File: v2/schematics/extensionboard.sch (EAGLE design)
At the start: 23 parts, among them IC1 TXS0104E, IC2 TXS0104E, IC3 TXS0104E, IC4 TXS0104E, IC5 TXS0104E_ENA, J1 Raspberry Pi 3, J10 RPi_GPIO_2, J11 I2C_2, J12 SPI1_5V, J13 SDA1_5V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

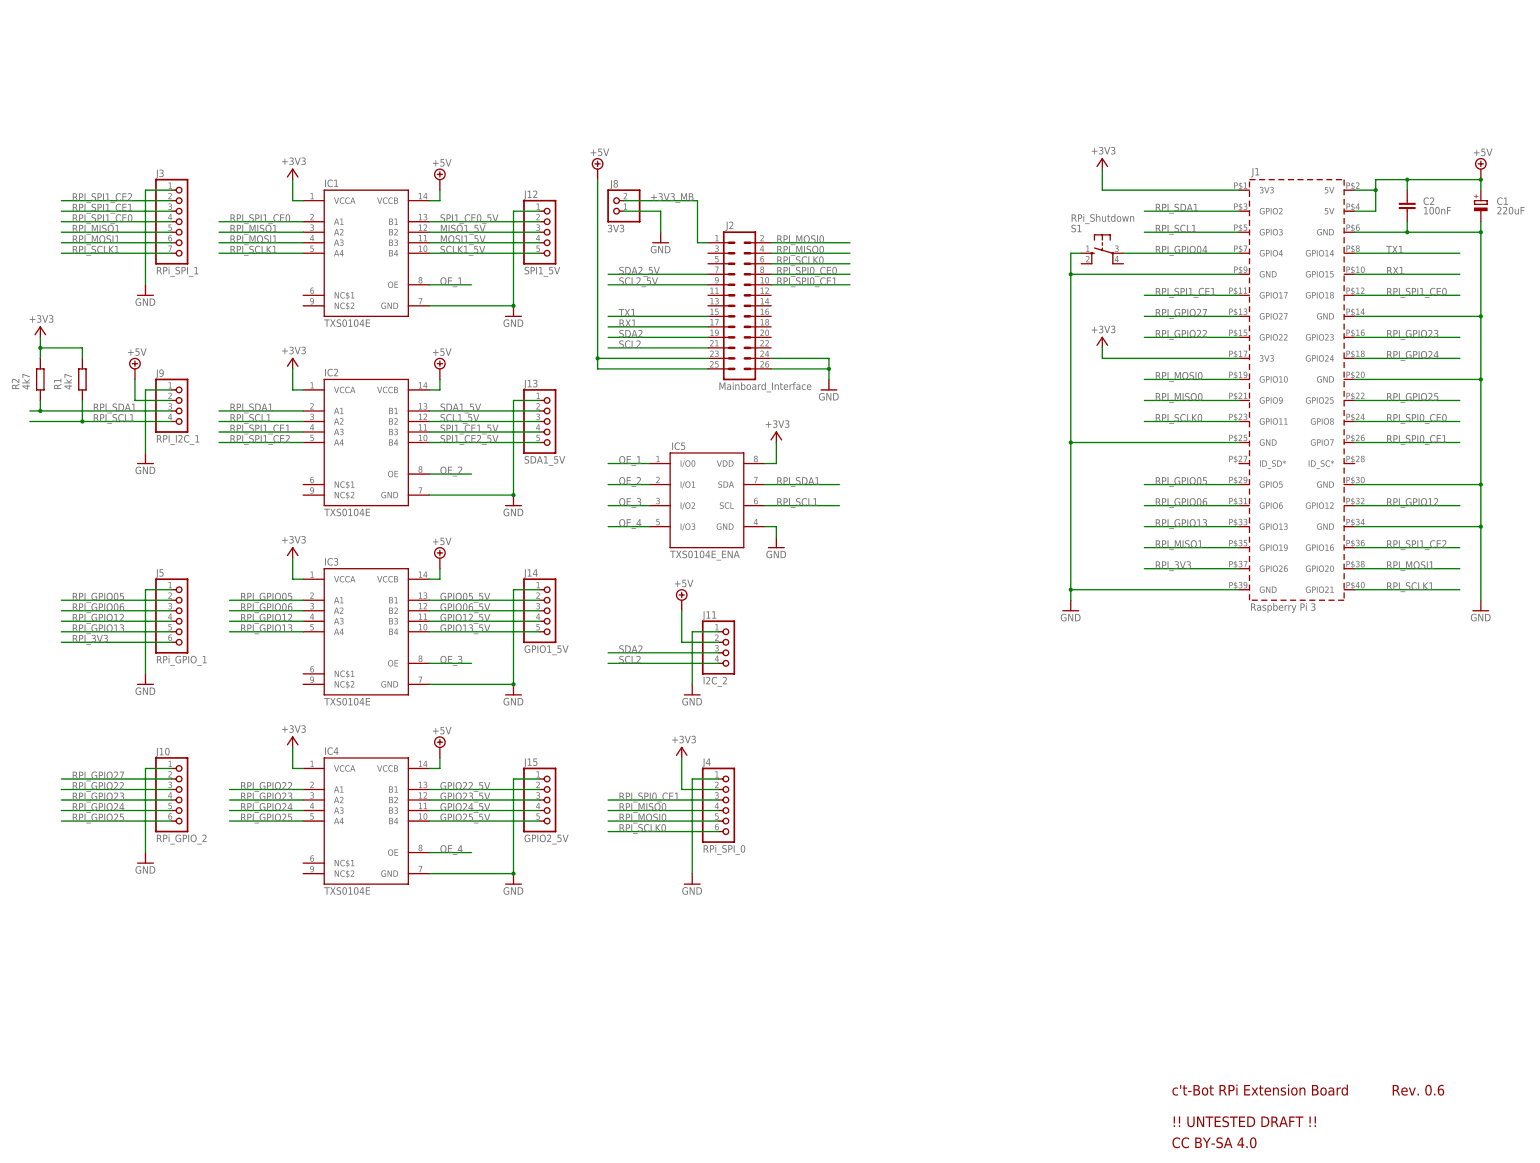
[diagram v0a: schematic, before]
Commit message: ct-bot v2 schematic updated
 - bugfix for library references, non-managed libraries added as dedicated library (ct-bot.lbr)
 - wrong footprints reverted
 - bufix for wrong signals for servo supplies
 - bugfix reverse polarity protection
 - bugifx for line sensor voltage levels
 - small smd parts exchanged with TH alternatives (bs108, mcp101) (untested)
 - distance and transport box sensors updated with I2C (untested)
 - led driver updated for up to 25 mA per channel (untested)
 - audio amp switched to pam8403 (untested)
 - bugfix for ESP12 programming mode (circuit still incomplete)
 - missing signals on RPi interface header restored
 - spi header for additional channels added due to pin mapping sheet changes
 - missing header for uart5 added
 - several layout improvements
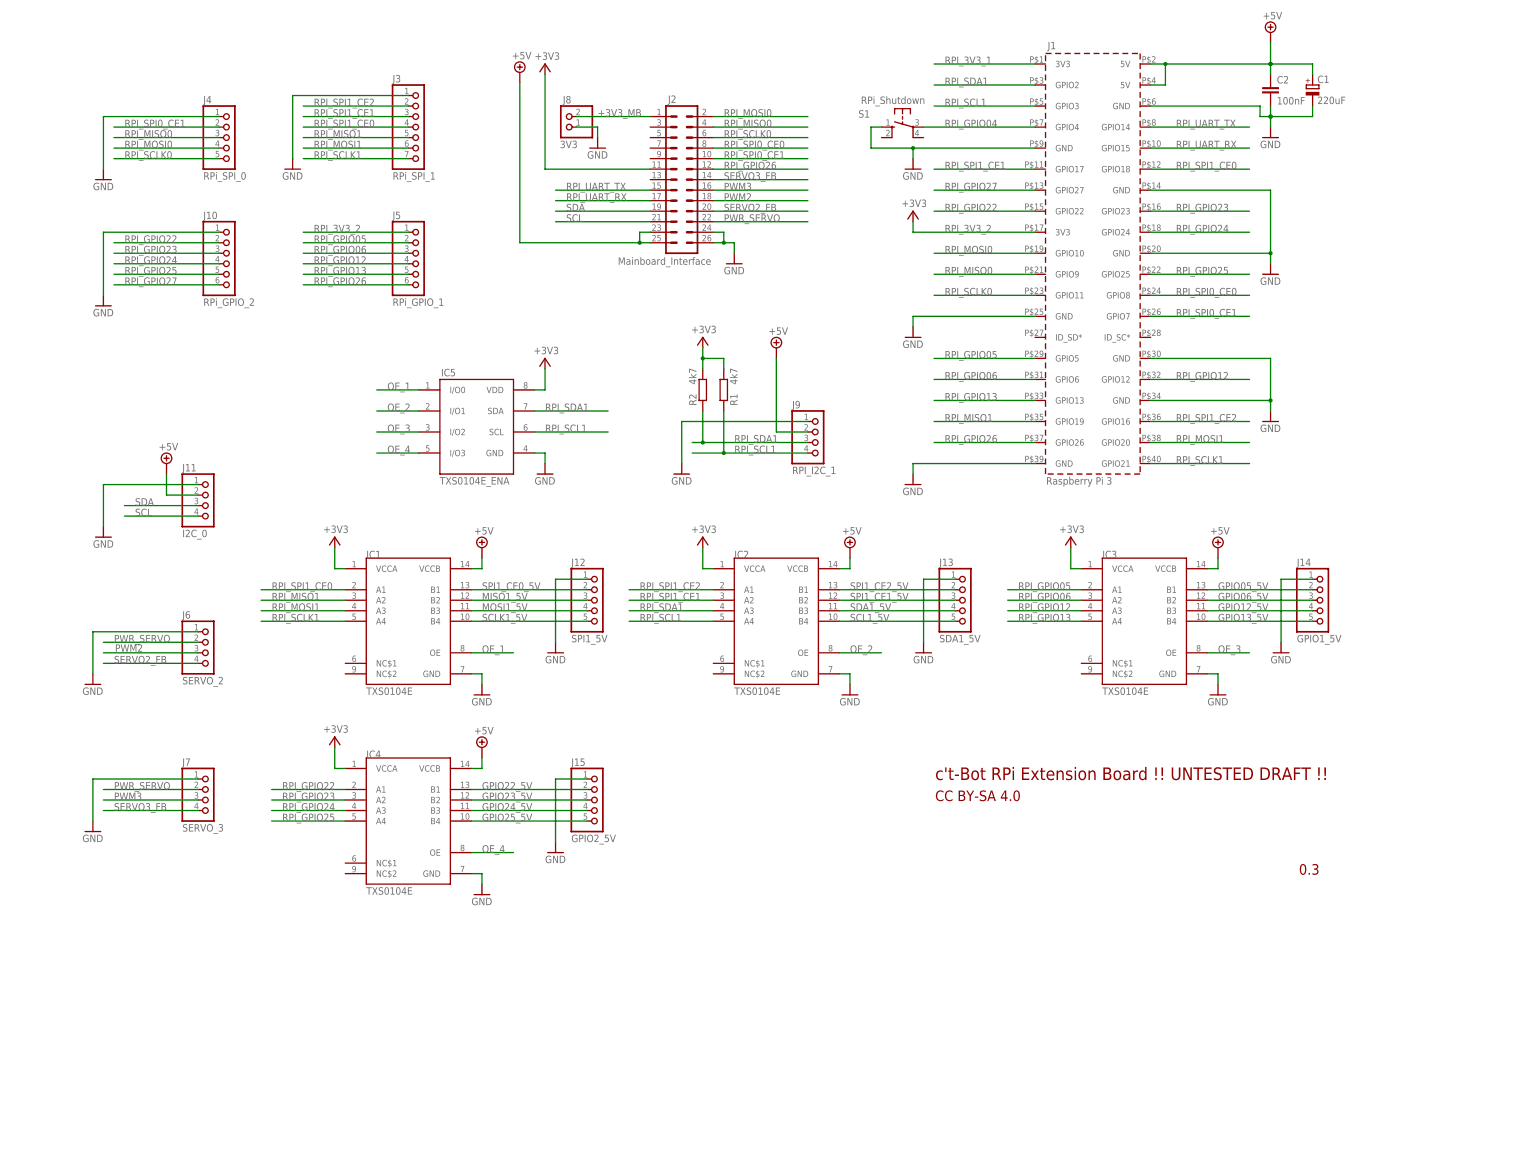
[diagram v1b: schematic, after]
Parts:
- added J6: SERVO_2, pinhead_ts:PINHD-1X4
- added J7: SERVO_3, pinhead_ts:PINHD-1X4
- J10, J5: device DIYmodules-pinhead:PINHD-1X6 -> pinhead_ts:PINHD-1X6
- J11: value I2C_2 -> I2C_0; device DIYmodules-pinhead:PINHD-1X4 -> pinhead_ts:PINHD-1X4
- J12, J13, J14, J15: device DIYmodules-pinhead:PINHD-1X5 -> pinhead_ts:PINHD-1X5
- J3: device DIYmodules-pinhead:PINHD-1X7 -> pinhead_ts:PINHD-1X7
- J4: device DIYmodules-pinhead:PINHD-1X6 -> pinhead_ts:PINHD-1X5
- J8: device DIYmodules-pinhead:PINHD-1X2 -> pinhead_ts:PINHD-1X2
- J9: device DIYmodules-pinhead:PINHD-1X4 -> pinhead_ts:PINHD-1X4
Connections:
- net N$1 renamed +3V3_MB
- net N$13 renamed SPI1_CE1_5V
- net N$14 renamed SDA1_5V
- net RX1 renamed RPI_UART_RX
- net SCL2 renamed SCL
- net SDA2 renamed SDA
- net TX1 renamed RPI_UART_TX
- removed net N$10: IC2.A2
- removed net N$11: IC2.A3
- removed net N$12: IC2.A4
- removed net N$2: J2.7
- removed net N$3: J2.9
- removed net N$4: J10.2
- removed net N$5: J10.3
- removed net N$6: J10.4
- removed net N$7: J10.5
- removed net N$8: J10.6
- removed net N$9: IC2.A1
- removed net RPI_3V3: J1.GPIO26, J5.6
- new net PWM2: J2.18, J6.3
- new net PWM3: J2.16, J7.3
- new net PWR_SERVO: J2.22, J6.2, J7.2
- new net RPI_GPIO26: J1.GPIO26, J2.12, J5.6
- new net SERVO2_FB: J2.20, J6.4
- new net SERVO3_FB: J2.14, J7.4
- net GND: now also J6.1, J7.1; no longer J5.1
- net RPI_3V3_1: no longer J4.2
- net RPI_3V3_2: now also J2.11, J5.1
- net RPI_GPIO22: now also J10.2
- net RPI_GPIO23: now also J10.3
- net RPI_GPIO24: now also J10.4
- net RPI_GPIO25: now also J10.5
- net RPI_GPIO27: now also J10.6
- net RPI_MISO0: now also J4.3; no longer J4.4
- net RPI_MOSI0: now also J4.4; no longer J4.5
- net RPI_SCL1: now also IC2.A4
- net RPI_SCLK0: now also J4.5; no longer J4.6
- net RPI_SDA1: now also IC2.A3
- net RPI_SPI0_CE1: now also J4.2; no longer J4.3
- net RPI_SPI1_CE1: now also IC2.A2
- net RPI_SPI1_CE2: now also IC2.A1
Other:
- note added: "0.3"
- note removed: "+3V3_MB"
- note removed: "RPI_GPIO22"
- note removed: "RPI_GPIO23"
- note removed: "RPI_GPIO24"
- note removed: "RPI_GPIO25"
- note removed: "RPI_GPIO27"
- note removed: "RPI_SCL1"
- note removed: "RPI_SDA1"
- note removed: "RPI_SPI1_CE1"
- note removed: "RPI_SPI1_CE2"
- note removed: "Rev. 0.6"
- note removed: "SCL1_5V"
- note removed: "SCL2_5V"
- note removed: "SDA1_5V"
- note removed: "SDA2_5V"
- note removed: "SPI1_CE1_5V"
- note removed: "SPI1_CE2_5V"
- moved on the sheet: C1, C2, IC1, IC2, IC3, IC4, IC5, J1, J10, J11, J12, J13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

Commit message: Updated schematics to Revision 0.6.
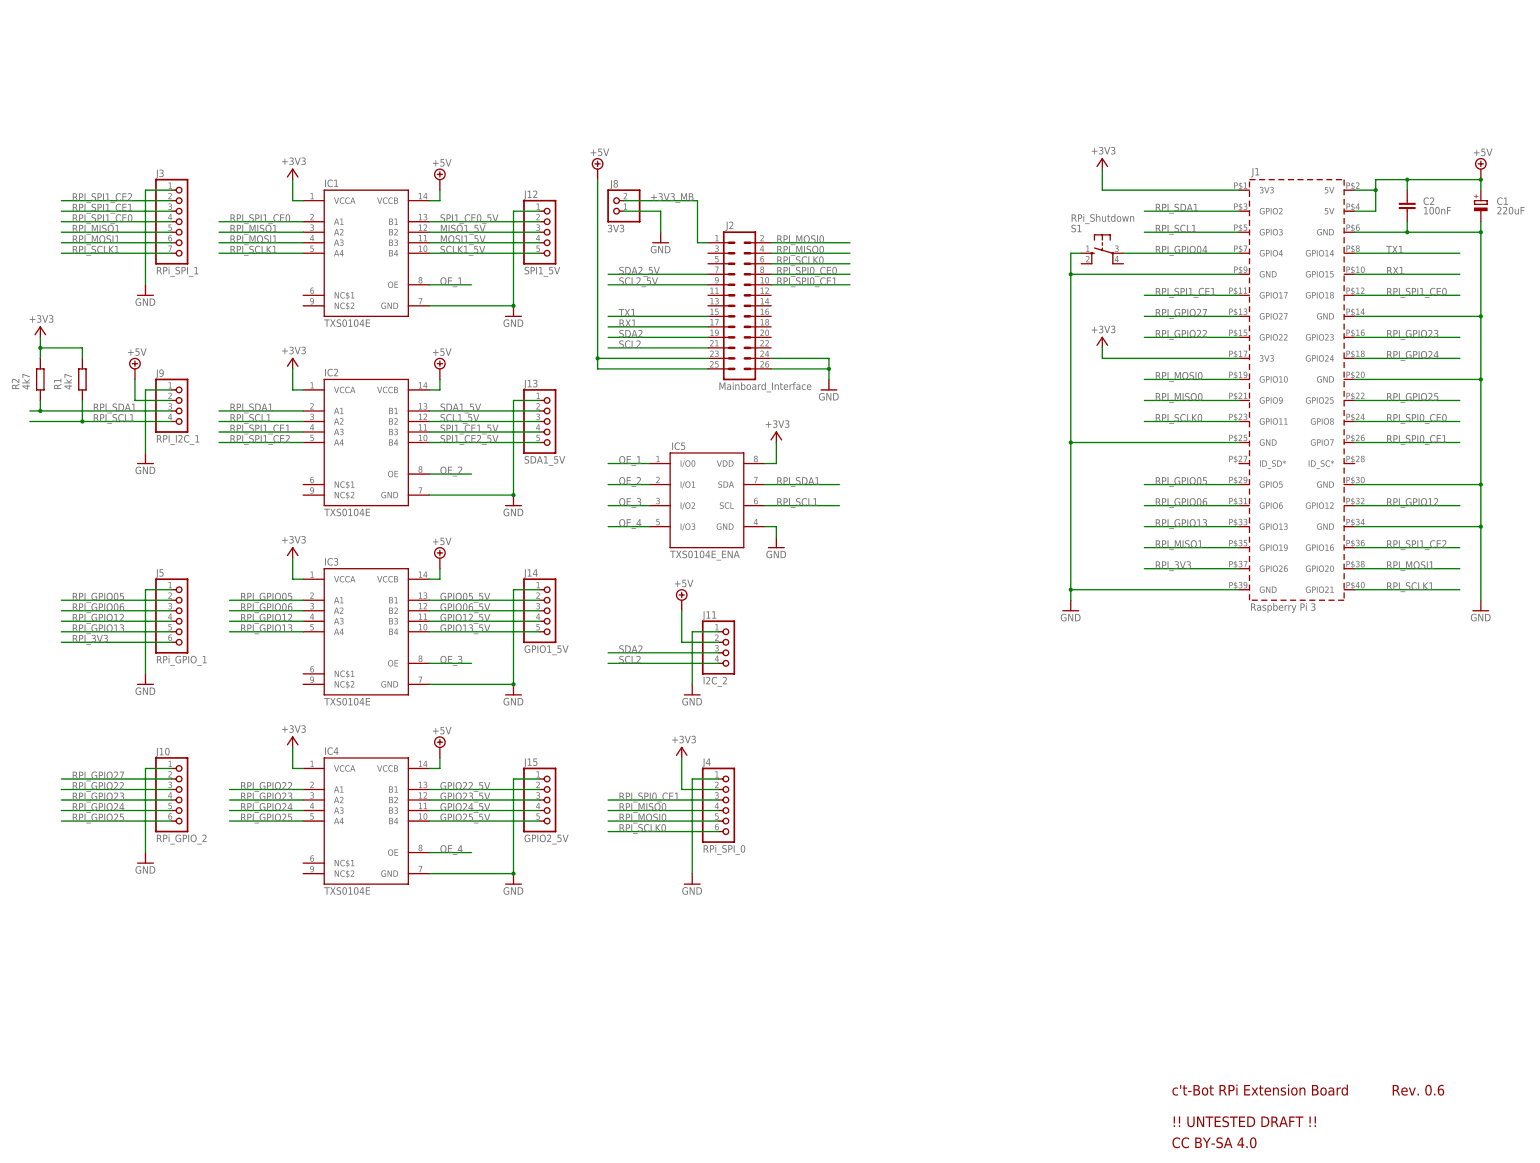
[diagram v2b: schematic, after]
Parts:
- removed J6: SERVO_2, pinhead_ts:PINHD-1X4
- removed J7: SERVO_3, pinhead_ts:PINHD-1X4
- J10, J5: device pinhead_ts:PINHD-1X6 -> DIYmodules-pinhead:PINHD-1X6
- J11: value I2C_0 -> I2C_2; device pinhead_ts:PINHD-1X4 -> DIYmodules-pinhead:PINHD-1X4
- J12, J13, J14, J15: device pinhead_ts:PINHD-1X5 -> DIYmodules-pinhead:PINHD-1X5
- J3: device pinhead_ts:PINHD-1X7 -> DIYmodules-pinhead:PINHD-1X7
- J4: device pinhead_ts:PINHD-1X5 -> DIYmodules-pinhead:PINHD-1X6
- J8: device pinhead_ts:PINHD-1X2 -> DIYmodules-pinhead:PINHD-1X2
- J9: device pinhead_ts:PINHD-1X4 -> DIYmodules-pinhead:PINHD-1X4
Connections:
- net +3V3_MB renamed N$1
- net RPI_UART_RX renamed RX1
- net RPI_UART_TX renamed TX1
- net SCL renamed SCL2
- net SDA renamed SDA2
- net SDA1_5V renamed N$14
- net SPI1_CE1_5V renamed N$13
- removed net PWM2: J2.18, J6.3
- removed net PWM3: J2.16, J7.3
- removed net PWR_SERVO: J2.22, J6.2, J7.2
- removed net RPI_GPIO26: J1.GPIO26, J2.12, J5.6
- removed net SERVO2_FB: J2.20, J6.4
- removed net SERVO3_FB: J2.14, J7.4
- new net N$10: IC2.A2
- new net N$11: IC2.A3
- new net N$12: IC2.A4
- new net N$2: J2.7
- new net N$3: J2.9
- new net N$4: J10.2
- new net N$5: J10.3
- new net N$6: J10.4
- new net N$7: J10.5
- new net N$8: J10.6
- new net N$9: IC2.A1
- new net RPI_3V3: J1.GPIO26, J5.6
- net GND: now also J5.1; no longer J6.1, J7.1
- net RPI_3V3_1: now also J4.2
- net RPI_3V3_2: no longer J2.11, J5.1
- net RPI_GPIO22: no longer J10.2
- net RPI_GPIO23: no longer J10.3
- net RPI_GPIO24: no longer J10.4
- net RPI_GPIO25: no longer J10.5
- net RPI_GPIO27: no longer J10.6
- net RPI_MISO0: now also J4.4; no longer J4.3
- net RPI_MOSI0: now also J4.5; no longer J4.4
- net RPI_SCL1: no longer IC2.A4
- net RPI_SCLK0: now also J4.6; no longer J4.5
- net RPI_SDA1: no longer IC2.A3
- net RPI_SPI0_CE1: now also J4.3; no longer J4.2
- net RPI_SPI1_CE1: no longer IC2.A2
- net RPI_SPI1_CE2: no longer IC2.A1
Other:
- note added: "+3V3_MB"
- note added: "RPI_GPIO22"
- note added: "RPI_GPIO23"
- note added: "RPI_GPIO24"
- note added: "RPI_GPIO25"
- note added: "RPI_GPIO27"
- note added: "RPI_SCL1"
- note added: "RPI_SDA1"
- note added: "RPI_SPI1_CE1"
- note added: "RPI_SPI1_CE2"
- note added: "Rev. 0.6"
- note added: "SCL1_5V"
- note added: "SCL2_5V"
- note added: "SDA1_5V"
- note added: "SDA2_5V"
- note added: "SPI1_CE1_5V"
- note added: "SPI1_CE2_5V"
- note removed: "0.3"
- moved on the sheet: C1, C2, IC1, IC2, IC3, IC4, IC5, J1, J10, J11, J12, J13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
